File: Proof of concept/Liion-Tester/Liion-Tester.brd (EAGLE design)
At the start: 89 x 42 mm, 24 parts, among them Q2 SI4403DDY-T1-GE3, U1 1042, U2 NCP1854FCCT1G, U3 BQ27427YZFR

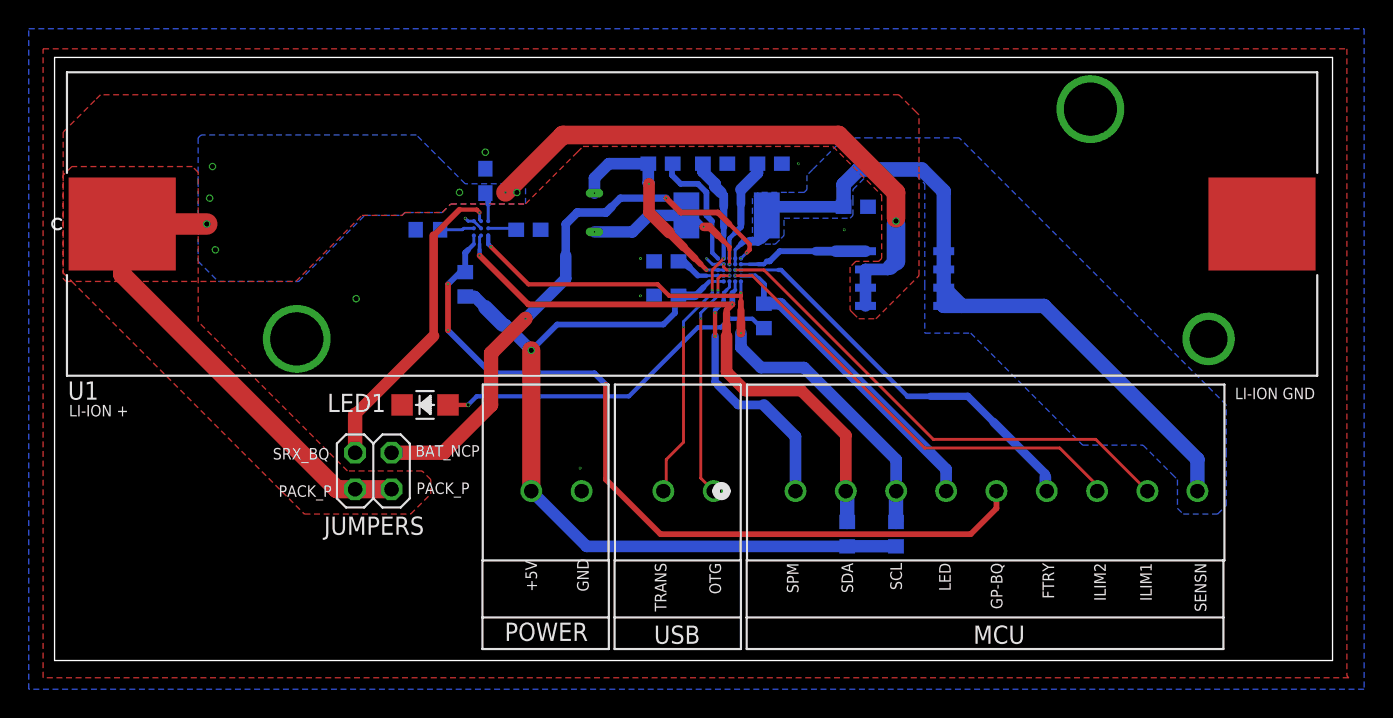
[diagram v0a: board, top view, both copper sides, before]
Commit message: Bigger vias and 4 layer pcb to order from JLCPCB
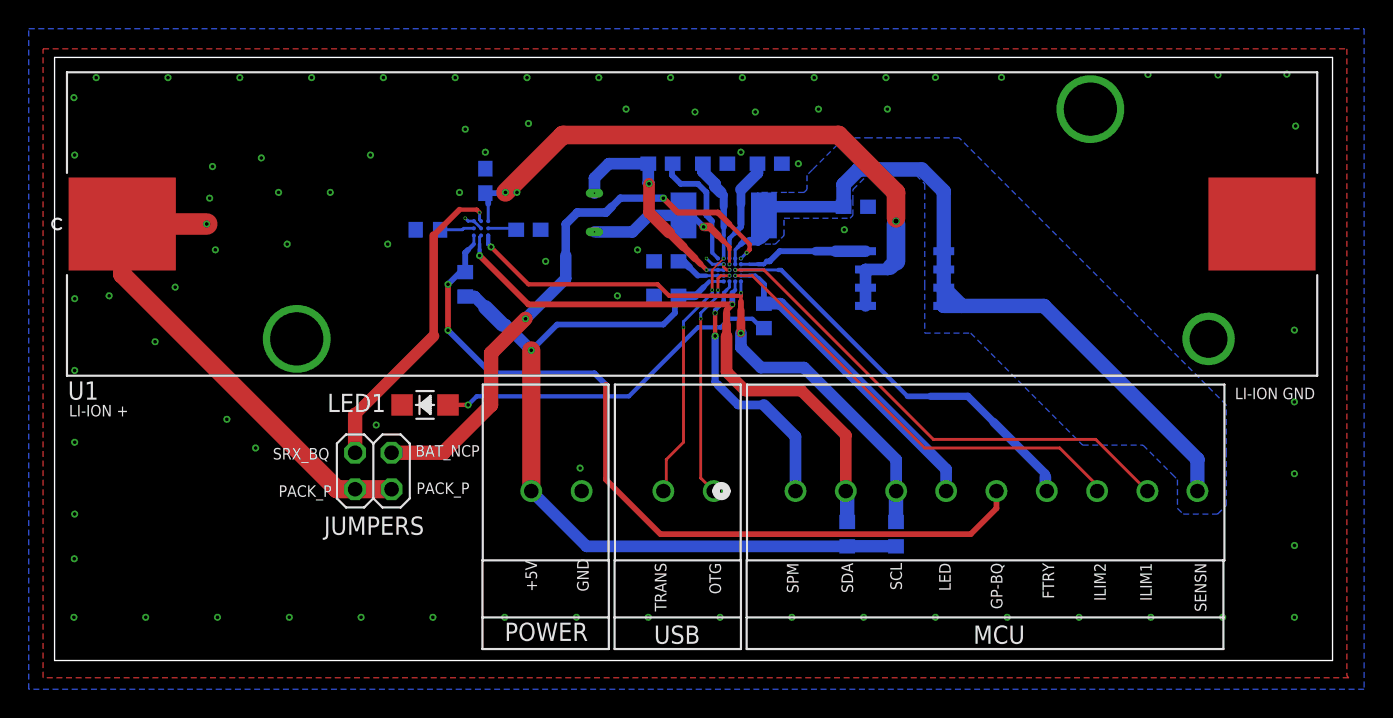
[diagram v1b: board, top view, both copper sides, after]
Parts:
- moved R6 0.20 mm to (57.6, 69.0)
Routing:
- net PACK_P: track 77.9 -> 79.3 mm, vias 8 -> 25
- net GND: vias 11 -> 61
- added copper zone on layer 2, net GND
- added copper zone on layer 15, net PACK_P
- removed copper zone on layer 1, net PACK_P
- removed copper zone on layer 16, net PACK_P
